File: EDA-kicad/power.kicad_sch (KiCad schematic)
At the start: 79 parts, among them SW6 CHP-041B, U10 BAT-CONNECTOR-FLTS22WR00, U11 BQ25792RQMR, U2 22V-boost-AP3032KTR-G1, U3 MP3429GL-Z, U4 TPS650250RHBR

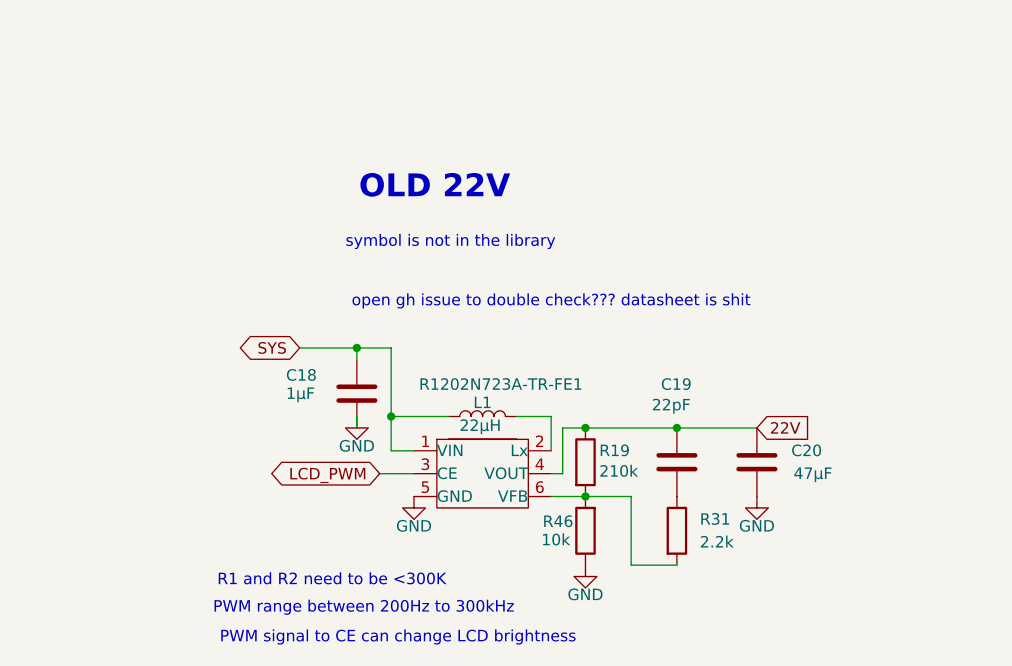
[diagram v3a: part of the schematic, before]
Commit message: delete old 22V rail
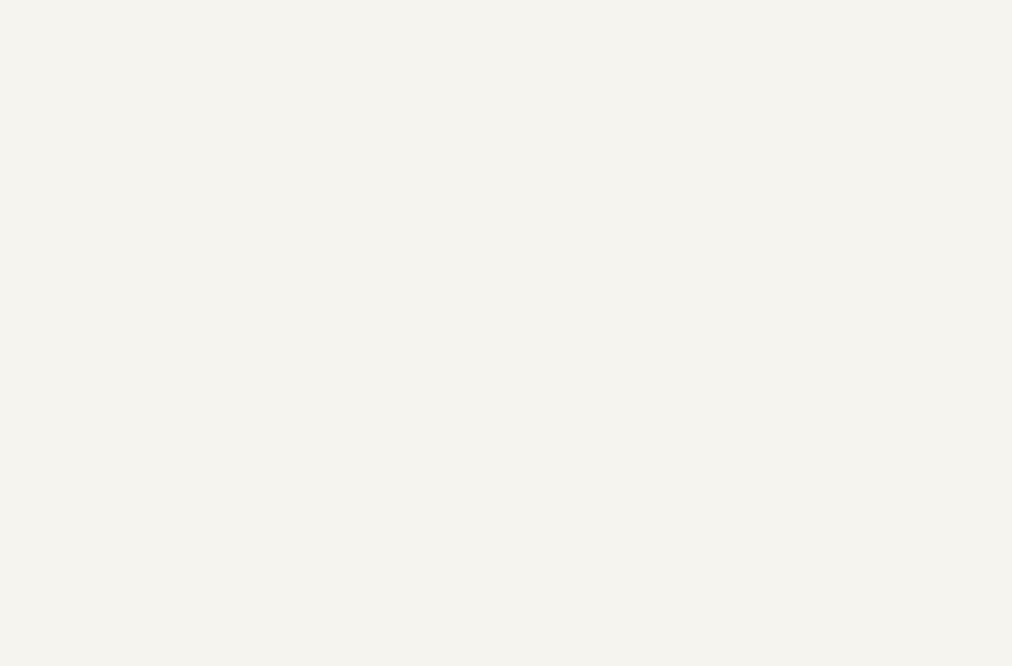
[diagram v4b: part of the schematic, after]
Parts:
- removed C18: 1μF, SPIRIT-footprints:0603-capacitor, symbol Device:C
- removed C19: 22pF, SPIRIT-footprints:0603-capacitor, symbol Device:C
- removed C20: 47µF, SPIRIT-footprints:C0805-capacitor, symbol Device:C
- removed L1: 22μH, symbol Device:L
- removed R1202N723A-TR-FE1: ~, Package_TO_SOT_SMD:TSOT-23-6, symbol R1202N723A-TR-FE:R1202N723A-TR-FE
- removed R19: 210k, symbol Device:R
- removed R31: 2.2k, symbol Device:R
- removed R46: 10k, SPIRIT-footprints:0603-resistor, symbol Device:R
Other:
- note removed: "OLD 22V"
- note removed: "PWM range between 200Hz to 300kHz"
- note removed: "PWM signal to CE can change LCD brightness"
- note removed: "R1 and R2 need to be <300K"
- note removed: "open gh issue to double check??? datasheet is shit"
- note removed: "symbol is not in the library"

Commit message: add placeholder symbols to 22V rail zener and r3
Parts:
- added D1: D_Zener, symbol Device:D_Zener
- added R9: R, symbol Device:R
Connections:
- net at L6.2, U2.1 (SW): now also D1.2 (A)
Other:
- moved on the sheet: C31, C32, L6, R20, R40, U2

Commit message: reannotate entire schematic
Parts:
- renumbered BAT2 to BAT1, C29 to C10, C55 to C15, C56 to C16, C5 to C17, C23 to C18, C17 to C19, C16 to C20, C15 to C21, C10 to C22, C67 to C23, C51 to C24, C27 to C25, C54 to C27, C65 to C28, C66 to C29, C32 to C30, C24 to C32, C61 to C33, C62 to C34, C63 to C35, C6 to C36, C58 to C37, C59 to C38, C60 to C39, C57 to C40, C30 to C41, C64 to C42, C21 to C7, C22 to C8, C53 to C9, L5 to L1, L8 to L2, L9 to L3, L10 to L4, L6 to L5, L7 to L6, Q11 to Q1, R43 to R10, R6 to R11, R16 to R12, R8 to R13, R7 to R14, R35 to R15, R36 to R16, R20 to R17, R9 to R18, R40 to R19, R39 to R20, R38 to R21, R37 to R22, R41 to R5, R45 to R6, R5 to R7, R42 to R8, R44 to R9, SW6 to SW1, U11 to U4, U4 to U5, U10 to U6, U2 to U7, U3 to U8
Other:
- note added: "LCD 22V 1.4A RAIL"
- note removed: "LCD 22V 700mA RAIL (?)"

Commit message: add schottky to 22V rail
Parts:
- removed D1: D_Zener, symbol Device:D_Zener
- added D3: D_Schottky, SPIRIT-footprints:schottky-diode-CR_DSN2_152AB-C_OSI, symbol Device:D_Schottky
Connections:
- net at L5.2, U7.1 (SW): now also D3.2 (A)
- net EN3V3A renamed EN3V3
- net EN3V3B renamed EN3V3EXT
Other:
- note added: "LCD power consumption: 900mW backlight + unknown W logic"
- note added: "TEST LCD POWER!!!!"
- note added: "datasheet problem - schottky instead of zener"
- note added: "schottky rated for 2A 40V"
- note added: "use testpads to determine"
- moved on the sheet: C37, C38, C39, R17, R19

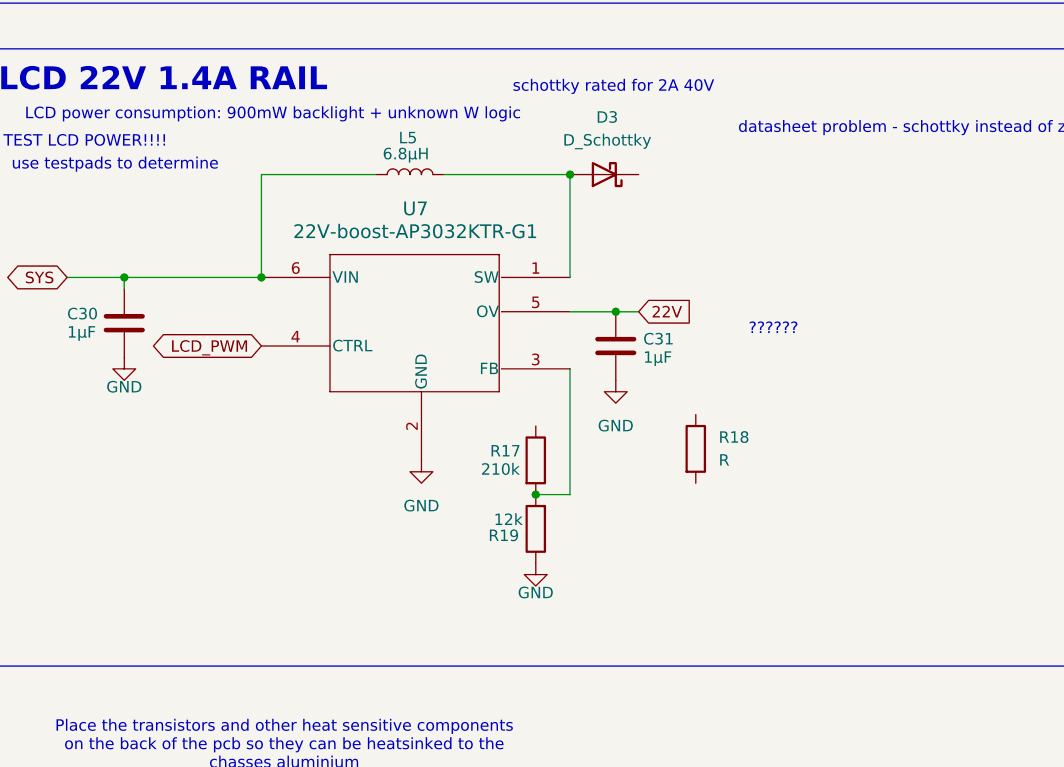
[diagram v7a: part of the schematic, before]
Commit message: finish 22V rail
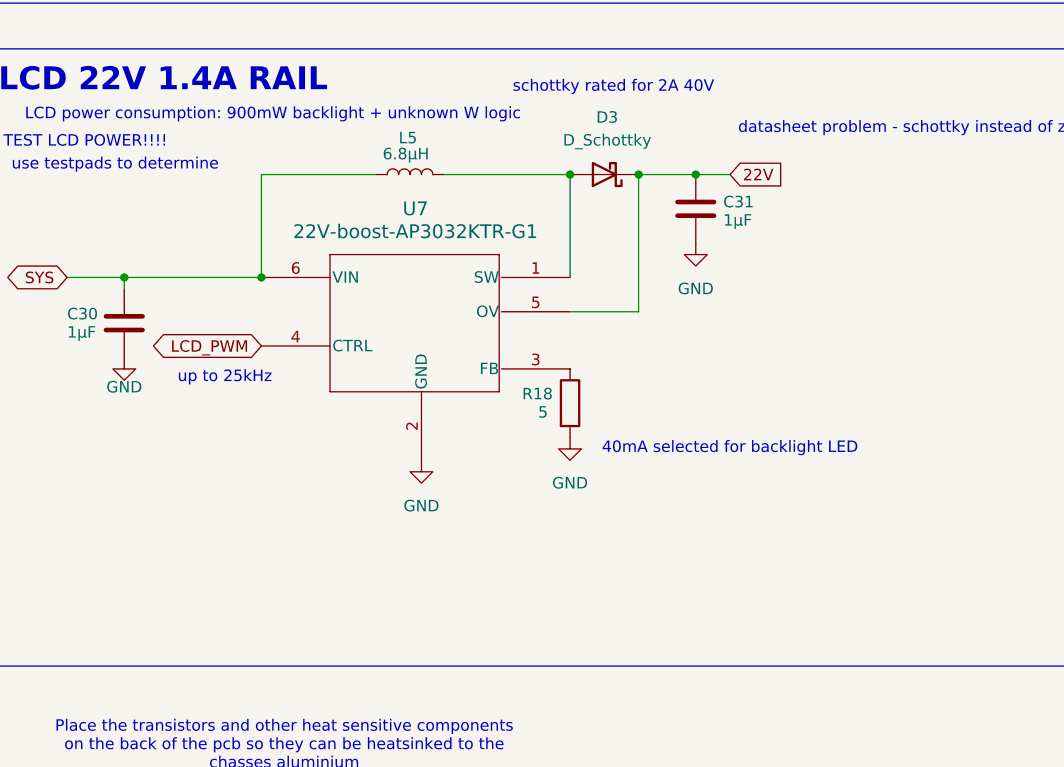
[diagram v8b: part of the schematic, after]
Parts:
- removed R17: 210k, symbol Device:R
- removed R19: 12k, SPIRIT-footprints:0603-resistor, symbol Device:R
- R18: value R -> 5; footprint (none) -> SPIRIT-footprints:0603-resistor; MPN (none) -> CSRT0603FT5R00
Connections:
- net 22V: now also D3.1 (K)
- net GND: now also R18.2
- net at U7.3 (FB): now also R18.1
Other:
- note added: "40mA selected for backlight LED"
- note added: "up to 25kHz"
- note removed: "??????"
- moved on the sheet: C31, R18
